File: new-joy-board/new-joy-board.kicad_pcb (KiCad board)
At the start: 2 copper layers, 61 x 139.2 mm, 43 parts, among them J0 SDS-50J, J1 SDS-50J, J2 SDS-50J, J3 SDS-50J, J4 BAT, U0 P82B715, U1 P82B715, U10 oskj-dc-dc, U2 P82B715, U3 P82B715, U4 AZReady_ESP32, U7 MPU6050_Breakout

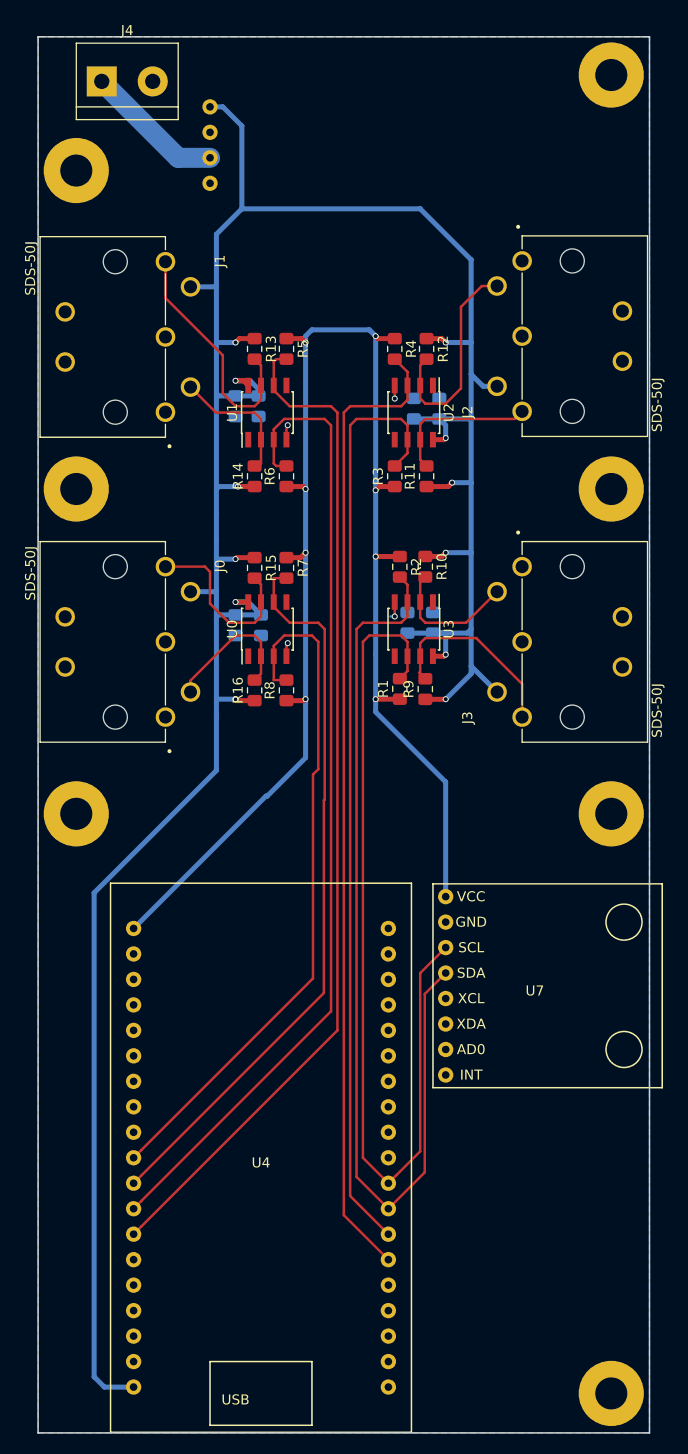
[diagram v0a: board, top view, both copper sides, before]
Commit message: Designed in the 24L01 board for emergency use
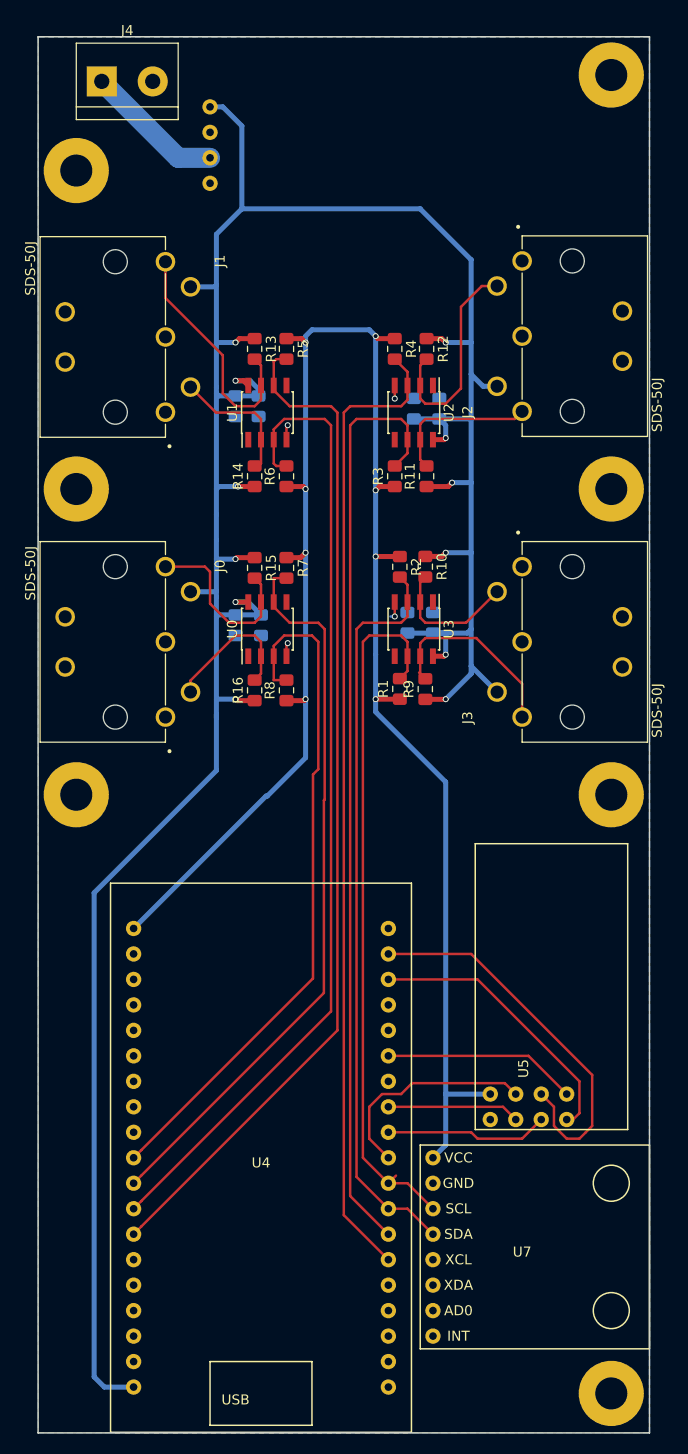
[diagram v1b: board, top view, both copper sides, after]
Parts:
- added U5: 24L01, new-joy:24L01, F.Cu at (127.6, 112.4)
- moved U7 26.1 mm to (124.5, 138.4)
- moved REF** 1.91 mm to (80.0, 93.3)
- moved REF** 1.91 mm to (133.3, 93.3)
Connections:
- U4 pad 29: Net-(U4-Pad29) -> /CS0
- U4 pad 30: Net-(U4-Pad30) -> /CLK
- U4 pad 31: Net-(U4-Pad31) -> /CE
- U4 pad 33: Net-(U4-Pad33) -> /IRQ
- U4 pad 36: Net-(U4-Pad36) -> /MISO
- U4 pad 37: Net-(U4-Pad37) -> /MOSI
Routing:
- net /MOSI: track 0.00 -> 39.0 mm
- net +3V3: track 149.6 -> 180.6 mm
- net /MISO: track 0.00 -> 28.0 mm
- net /CS0: track 0.00 -> 21.9 mm
- net /SDA3ESP: track 94.8 -> 74.4 mm
- net /IRQ: track 0.00 -> 19.4 mm
- net /SCL3ESP: track 89.8 -> 70.6 mm
- net /CLK: track 0.00 -> 16.3 mm
- net /CE: track 0.00 -> 13.2 mm

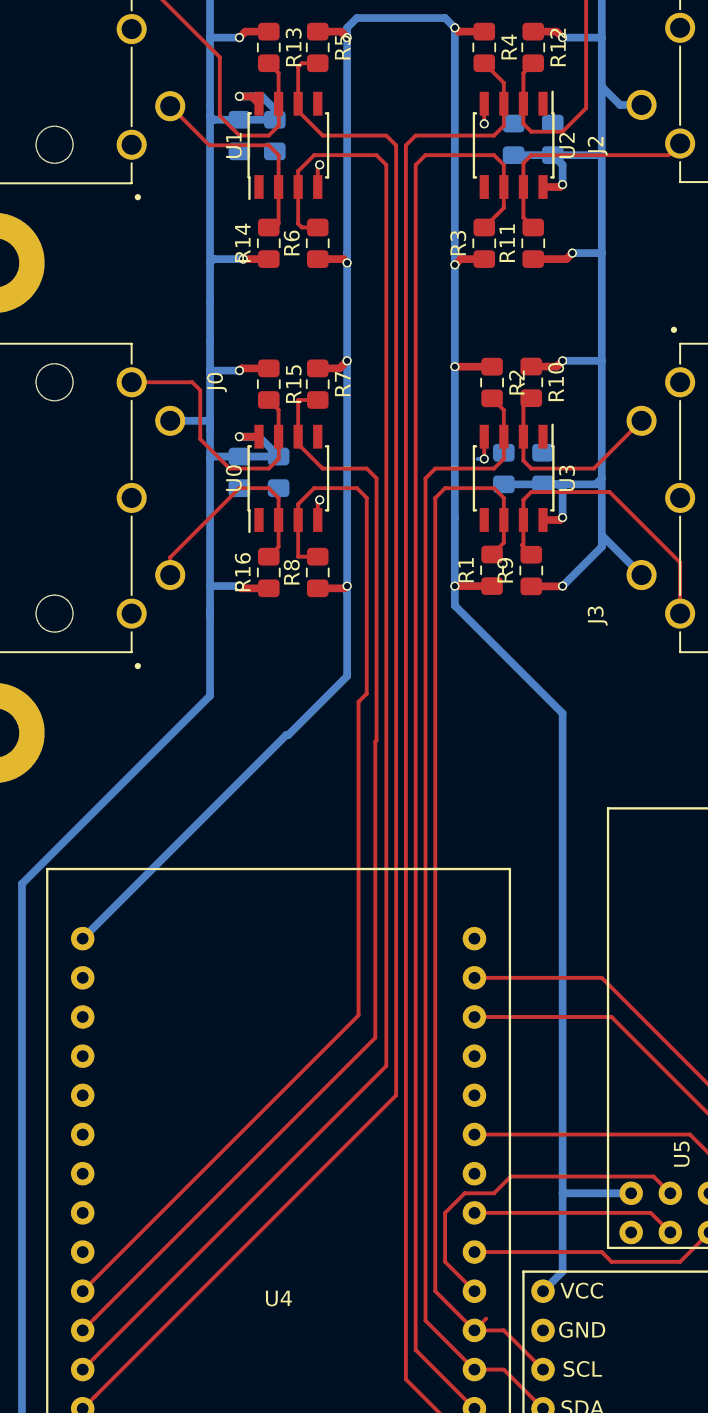
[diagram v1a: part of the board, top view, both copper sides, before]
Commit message: Replaced the 1uF with 47uF Elekos as per David's recommendation
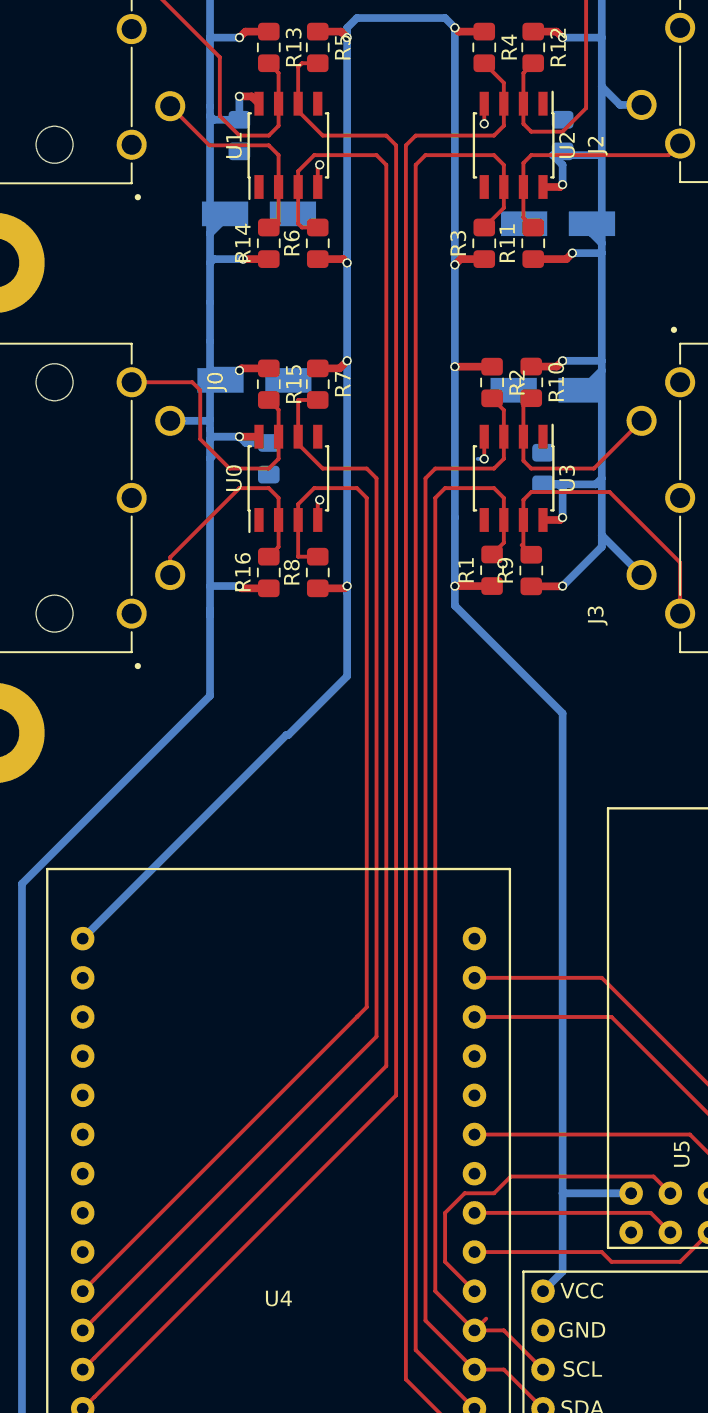
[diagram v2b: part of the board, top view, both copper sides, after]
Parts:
- C5, C6, C7, C8: value 1uF -> 47uF; footprint Capacitor_SMD:C_0805_2012Metric_Pad1.15x1.40mm_HandSolder -> Capacitor_SMD:CP_Elec_5x5.8
- moved C5 6.04 mm to (96.9, 70.5), turned to 0 degrees
- moved C8 5.82 mm to (115.9, 71.1), turned to 180 degrees
- moved C7 5.48 mm to (116.5, 60.3), turned to 180 degrees
- moved C6 5.18 mm to (97.2, 59.7), turned to 0 degrees
- moved C3 3.18 mm to (116.8, 54.6)
- moved C1 1.09 mm to (97.8, 75.6)
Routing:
- net +5V: track 291.2 -> 283.8 mm
